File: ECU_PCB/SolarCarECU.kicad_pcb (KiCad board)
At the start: 4 copper layers, 160 x 105.4 mm, 185 parts, among them J2 Screw_Terminal_01x08, J3 Screw_Terminal_01x08, J4 Screw_Terminal_01x08, J5 Screw_Terminal_01x08, J6 Screw_Terminal_01x08, J7 Screw_Terminal_01x08, J8 Screw_Terminal_01x08, Q1 QM6015D, Q2 QM6015D, Q3 QM6015D, Q4 QM6015D, Q5 QM6015D, Q6 QM6015D, Q7 QM6015D, U1 Teensy3.6, U10 LM324A, U11 MCP1403, U2 MCP1403, U3 MCP1403, U4 L7805, U5 MCP2562-E-P, U6 MCP2562-E-P, U7 4504, U8 4504, U9 4504

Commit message: laid tracks for fuses in pcb. bypass capacitors are not clearing rats nest for some reason...is this a problem?
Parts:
- removed C1: 470uF, Capacitor_THT:CP_Radial_D13.0mm_P5.00mm
- added F1: Polyfuse, Fuse:Fuse_0603_1608Metric, F.Cu at (184.3, 96.5)
- added F10: Polyfuse, Fuse:Fuse_0603_1608Metric, B.Cu at (127.3, 107.2)
- added F11: Polyfuse, Fuse:Fuse_0603_1608Metric, B.Cu at (124.7, 107.2)
- added F12: Polyfuse, Fuse:Fuse_0603_1608Metric, F.Cu at (122.2, 107.2)
- added F13: Polyfuse, Fuse:Fuse_0603_1608Metric, F.Cu at (119.6, 107.2)
- added F14: Polyfuse, Fuse:Fuse_0603_1608Metric, F.Cu at (117.1, 107.2)
- added F15: Polyfuse, Fuse:Fuse_0603_1608Metric, F.Cu at (114.6, 107.2)
- added F16: Polyfuse, Fuse:Fuse_0603_1608Metric, F.Cu at (110.0, 112.2)
- added F17: Polyfuse, Fuse:Fuse_0603_1608Metric, F.Cu at (112.0, 112.2)
- added F18: Polyfuse, Fuse:Fuse_0603_1608Metric, F.Cu at (110.4, 124.7)
- added F19: Polyfuse, Fuse:Fuse_0603_1608Metric, B.Cu at (142.5, 133.3)
- added F2: Polyfuse, Fuse:Fuse_0603_1608Metric, F.Cu at (184.3, 98.9)
- added F20: Polyfuse, Fuse:Fuse_0603_1608Metric, B.Cu at (145.0, 133.5)
- added F21: Polyfuse, Fuse:Fuse_0603_1608Metric, B.Cu at (147.6, 133.5)
- added F22: Polyfuse, Fuse:Fuse_0603_1608Metric, B.Cu at (156.6, 102.0)
- added F23: Polyfuse, Fuse:Fuse_0603_1608Metric, B.Cu at (151.5, 107.3)
- added F24: Polyfuse, Fuse:Fuse_0603_1608Metric, B.Cu at (153.9, 131.6)
- added F25: Polyfuse, Fuse:Fuse_0603_1608Metric, B.Cu at (146.8, 121.2)
- added F26: Polyfuse, Fuse:Fuse_0603_1608Metric, F.Cu at (110.5, 120.0)
- added F27: Polyfuse, Fuse:Fuse_0603_1608Metric, B.Cu at (123.4, 102.8)
- added F28: Polyfuse, Fuse:Fuse_0603_1608Metric, B.Cu at (126.0, 102.8)
- added F29: Polyfuse, Fuse:Fuse_0603_1608Metric, B.Cu at (126.0, 129.8)
- added F3: Polyfuse, Fuse:Fuse_0603_1608Metric, B.Cu at (165.6, 106.8)
- added F30: Polyfuse, Fuse:Fuse_0603_1608Metric, B.Cu at (123.4, 129.8)
- added F31: Polyfuse, Fuse:Fuse_0603_1608Metric, B.Cu at (120.9, 129.9)
- added F32: Polyfuse, Fuse:Fuse_0603_1608Metric, B.Cu at (118.4, 129.9)
- added F33: Polyfuse, Fuse:Fuse_0603_1608Metric, B.Cu at (128.7, 102.8)
- added F34: Polyfuse, Fuse:Fuse_0603_1608Metric, B.Cu at (131.1, 102.8)
- added F35: Polyfuse, Fuse:Fuse_0603_1608Metric, B.Cu at (133.7, 102.8)
- added F36: Polyfuse, Fuse:Fuse_0603_1608Metric, B.Cu at (159.0, 136.7)
- added F37: Polyfuse, Fuse:Fuse_0603_1608Metric, B.Cu at (162.8, 121.2)
- added F38: Polyfuse, Fuse:Fuse_0603_1608Metric, B.Cu at (178.3, 110.9)
- added F39: Polyfuse, Fuse:Fuse_0603_1608Metric, F.Cu at (166.6, 103.7)
- added F4: Polyfuse, Fuse:Fuse_0603_1608Metric, B.Cu at (155.2, 107.3)
- added F40: Polyfuse, Fuse:Fuse_0603_1608Metric, B.Cu at (160.3, 133.6)
- added F41: Polyfuse, Fuse:Fuse_0603_1608Metric, B.Cu at (157.7, 133.6)
- added F42: Polyfuse, Fuse:Fuse_0603_1608Metric, F.Cu at (180.8, 122.6)
- added F43: Polyfuse, Fuse:Fuse_0603_1608Metric, F.Cu at (180.8, 120.9)
- added F44: Polyfuse, Fuse:Fuse_0603_1608Metric, B.Cu at (150.1, 133.5)
- added F5: Polyfuse, Fuse:Fuse_0603_1608Metric, B.Cu at (156.5, 129.5)
- added F6: Polyfuse, Fuse:Fuse_0603_1608Metric, B.Cu at (151.4, 115.4)
- added F7: Polyfuse, Fuse:Fuse_0603_1608Metric, B.Cu at (134.9, 107.2)
- added F8: Polyfuse, Fuse:Fuse_0603_1608Metric, B.Cu at (132.3, 107.2)
- added F9: Polyfuse, Fuse:Fuse_0603_1608Metric, B.Cu at (129.8, 107.2)
- added R55: 100k, Resistor_SMD:R_0603_1608Metric, B.Cu at (215.6, 87.1)
- added R95: 0, Resistor_SMD:R_0603_1608Metric, F.Cu at (133.5, 129.5)
- C44: moved to B.Cu
- moved C44 24.4 mm to (181.3, 110.1), turned to 0 degrees
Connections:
- net /CS_0 renamed Net-(U1-Pad12)
- net /CS_2 renamed Net-(U1-Pad70)
- net /MISO_0 renamed Net-(U1-Pad13)
- net /MISO_2 renamed Net-(U1-Pad72)
- net /MOSI_0 renamed Net-(U1-Pad14)
- net /MOSI_2 renamed Net-(U1-Pad71)
- net /SCK_2 renamed Net-(U1-Pad73)
- net /USB_D+ renamed Net-(U1-Pad60)
- net /USB_D- renamed Net-(U1-Pad59)
- U1 pad 10: /UART_3_TX -> Net-(F6-Pad1)
- U1 pad 16: /LV_HAZARD_CTRL -> Net-(F7-Pad1)
- U1 pad 17: /LV_HAZARD_LED -> Net-(F8-Pad1)
- U1 pad 18: /LV_DOWN_CTRL -> Net-(F9-Pad1)
- U1 pad 19: /LV_UP_CTRL -> Net-(F10-Pad1)
- U1 pad 2: /UART_1_RX -> Net-(F1-Pad1)
- U1 pad 20: /LV_SEL_CTRL -> Net-(F11-Pad1)
- U1 pad 21: /CAN0_TX -> Net-(F12-Pad1)
- U1 pad 22: /CAN0_RX -> Net-(F13-Pad1)
- U1 pad 23: /UART_4_RX -> Net-(F14-Pad1)
- U1 pad 24: /UART_4_TX -> Net-(F15-Pad1)
- U1 pad 3: /UART_1_TX -> Net-(F2-Pad1)
- U1 pad 30: /CAN1_TX -> Net-(F16-Pad1)
- U1 pad 31: /CAN1_RX -> Net-(F17-Pad1)
- U1 pad 36: /LV_MOTOR_R_ECO_EN -> Net-(F18-Pad1)
- U1 pad 4: /LV_KILL_SENSE -> Net-(F3-Pad1)
- U1 pad 41: /LV_GEARSHIFT_CTRL -> Net-(F19-Pad1)
- U1 pad 42: /LV_TURNSIG_CTRL -> Net-(F20-Pad1)
- U1 pad 43: /LV_THROTTLE_CTRL -> Net-(F21-Pad1)
- U1 pad 44: /LV_REGEN_CTRL -> Net-(F44-Pad2)
- U1 pad 45: /SDA_0 -> Net-(F43-Pad2)
- U1 pad 46: /SCL_0 -> Net-(F42-Pad2)
- U1 pad 47: /LV_BRAKE_CTRL -> Net-(F41-Pad2)
- U1 pad 48: /LV_STEER_CTRL -> Net-(F40-Pad2)
- U1 pad 49: /LV_HORN_CTRL -> Net-(F39-Pad2)
- U1 pad 50: /LV_HEADLIGHT_CTRL -> Net-(F38-Pad2)
- U1 pad 56: /LV_MOTOR_R_METER -> Net-(F37-Pad2)
- U1 pad 57: /LV_MOTOR_L_METER -> Net-(F36-Pad2)
- U1 pad 67: /LV_LEFT_BLINKERS -> Net-(F35-Pad2)
- U1 pad 68: /LV_RIGHT_BLINKERS -> Net-(F34-Pad2)
- U1 pad 69: /LV_HEADLIGHTS -> Net-(F33-Pad2)
- U1 pad 76: /UART_6_RX -> Net-(F32-Pad2)
- U1 pad 77: /UART_6_TX -> Net-(F31-Pad2)
- U1 pad 78: /LV_MOTOR_L_ECO_EN -> Net-(F30-Pad2)
- U1 pad 79: /LV_MOTOR_L_REGEN_EN -> Net-(F29-Pad2)
- U1 pad 8: /LV_STROBE -> Net-(F4-Pad1)
- U1 pad 80: /LV_MOTOR_R_REV_EN -> Net-(F28-Pad2)
- U1 pad 81: /LV_MOTOR_R_FWD_EN -> Net-(F27-Pad2)
- U1 pad 82: /LV_MOTOR_R_REGEN_EN -> Net-(F26-Pad2)
- U1 pad 83: /LV_MOTOR_L_REV_EN -> Net-(F25-Pad2)
- U1 pad 84: /LV_MOTOR_L_FWD_EN -> Net-(F24-Pad2)
- U1 pad 85: /LV_BRAKELIGHTS -> Net-(F23-Pad2)
- U1 pad 86: /LV_HORN -> Net-(F22-Pad2)
- U1 pad 9: /UART_3_RX -> Net-(F5-Pad1)
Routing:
- net Net-(F43-Pad2): track 0.00 -> 29.6 mm
- net /SDA_0: track 124.1 -> 96.1 mm
- net /LV_MOTOR_R_FWD_EN: track 79.7 -> 51.8 mm
- net /LV_MOTOR_R_REGEN_EN: track 67.1 -> 40.4 mm
- net /SCL_0: track 121.1 -> 94.6 mm
- net Net-(F42-Pad2): track 0.00 -> 26.4 mm
- net Net-(F27-Pad2): track 0.00 -> 26.4 mm
- net Net-(F26-Pad2): track 0.00 -> 26.1 mm
- net /LV_HEADLIGHT_CTRL: track 81.2 -> 55.5 mm, vias 3 -> 1
- net /LV_HORN_CTRL: track 83.0 -> 58.0 mm, vias 3 -> 2
- net Net-(F39-Pad2): track 0.00 -> 23.4 mm, vias 0 -> 1
- net /UART_1_RX: track 49.9 -> 27.0 mm, vias 1 -> 0
- net Net-(F38-Pad2): track 0.00 -> 22.3 mm, vias 0 -> 2
- net /UART_1_TX: track 49.1 -> 27.1 mm
- net /LV_MOTOR_R_REV_EN: track 77.5 -> 56.1 mm
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
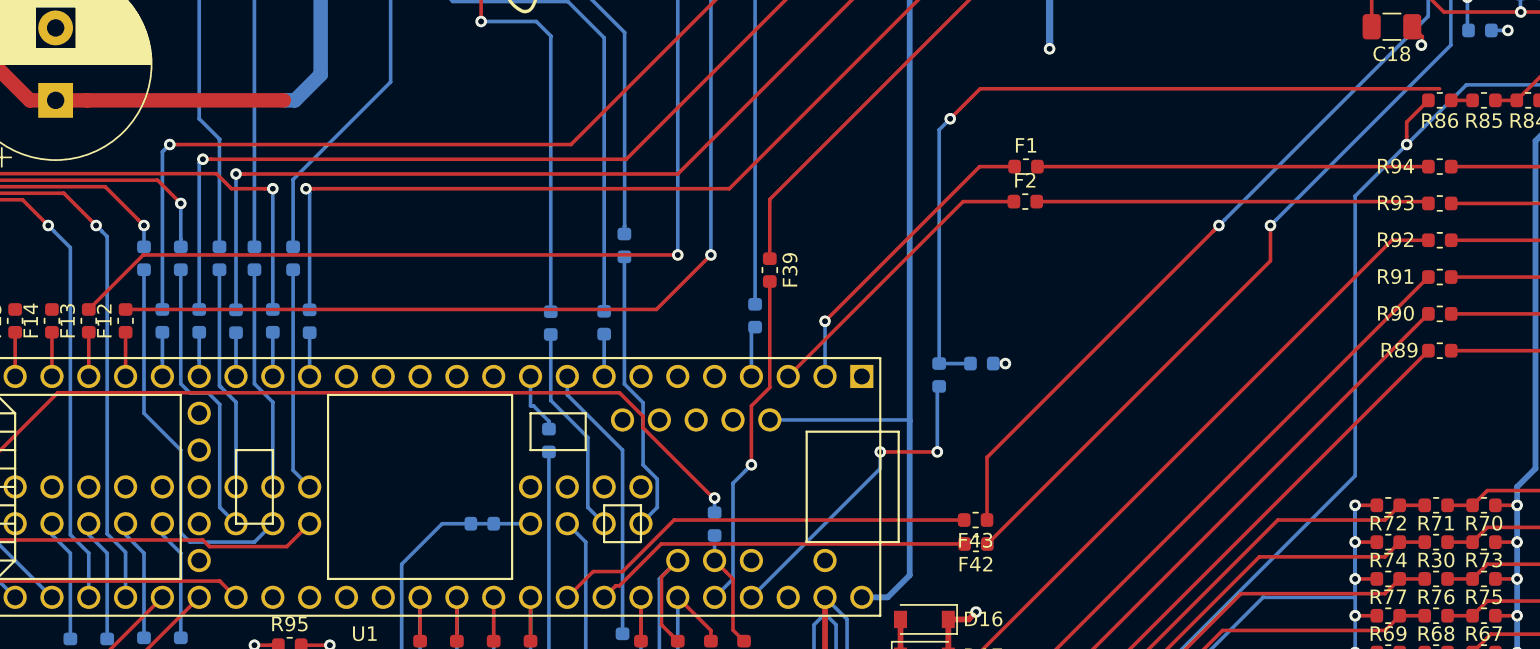
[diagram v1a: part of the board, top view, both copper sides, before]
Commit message: fix a couple traces
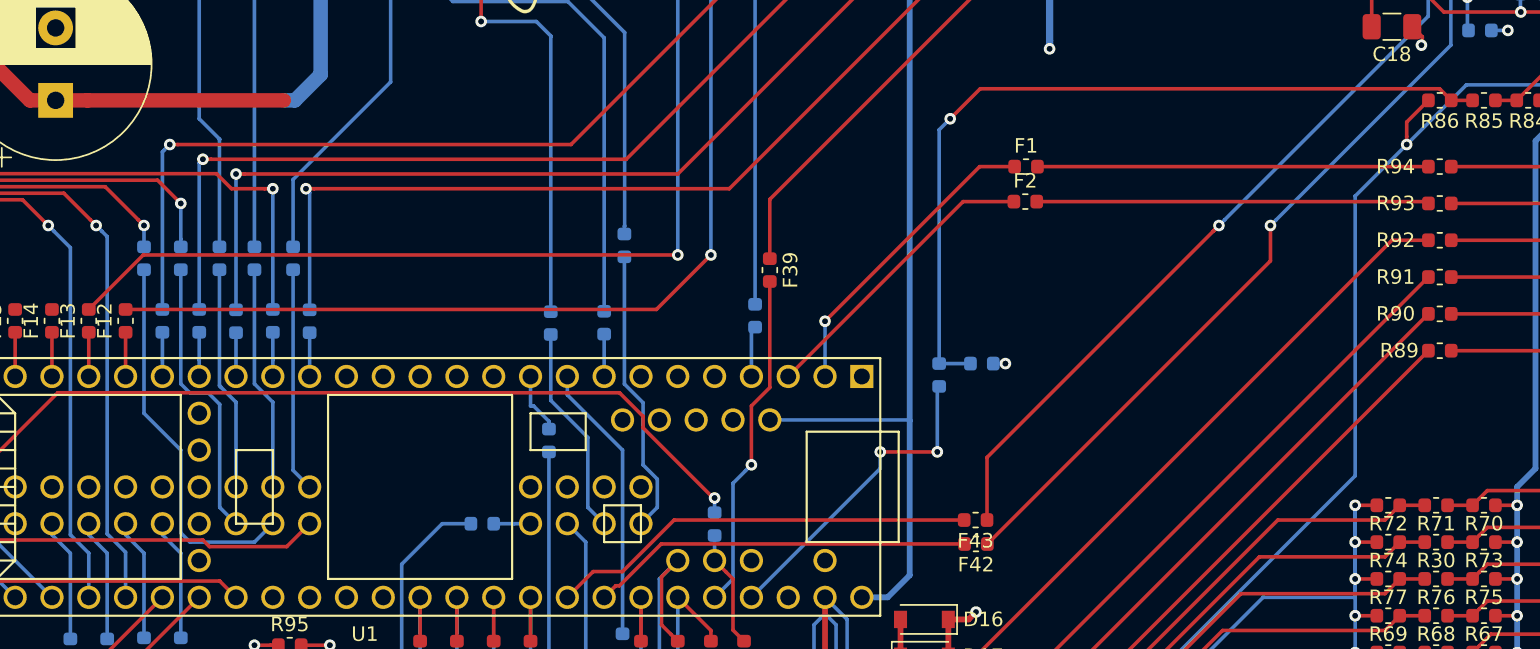
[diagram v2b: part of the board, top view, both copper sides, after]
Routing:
- net /LV_MOTOR_L_REV_EN: track 81.3 -> 77.2 mm
- net Net-(F25-Pad2): track 0.00 -> 2.54 mm
- net /LV_HEADLIGHT_CTRL: track 55.5 -> 56.6 mm
- net Net-(F13-Pad1): track 2.54 -> 3.05 mm
- net Net-(F12-Pad1): track 2.54 -> 3.05 mm

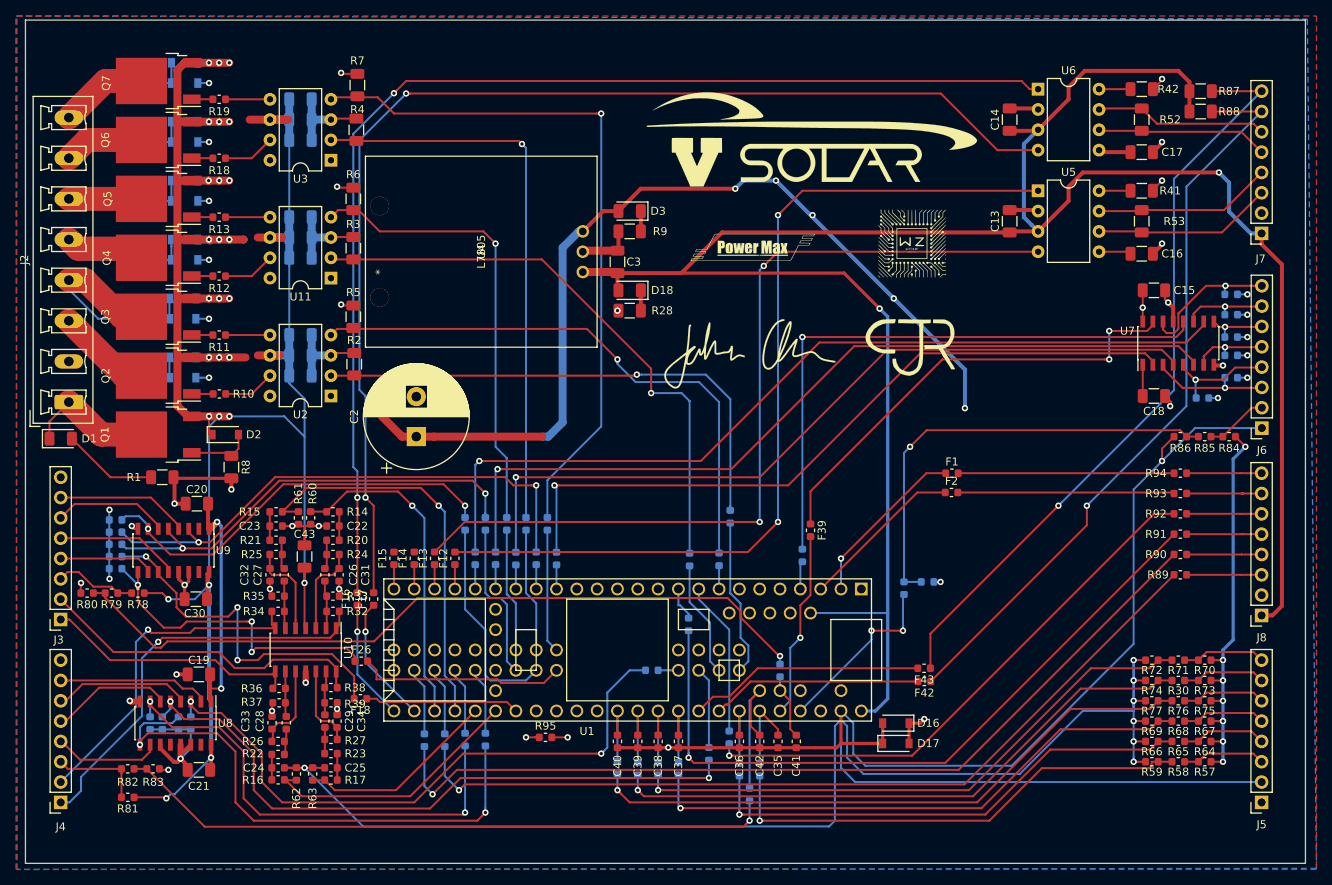
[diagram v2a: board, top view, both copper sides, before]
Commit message: fixed drc and routing errors
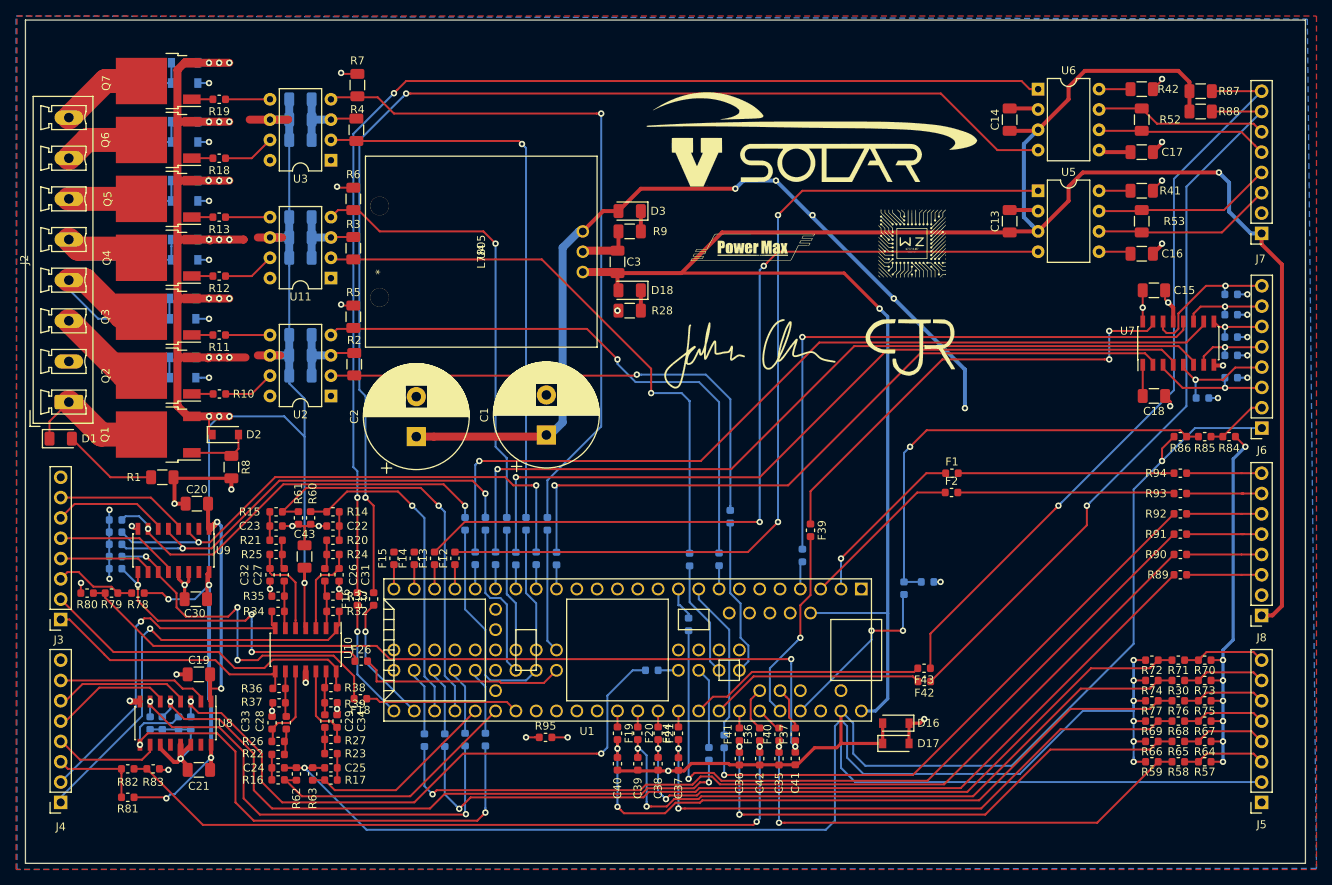
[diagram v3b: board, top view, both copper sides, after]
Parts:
- added C1: 470uF, Capacitor_THT:CP_Radial_D13.0mm_P5.00mm, F.Cu at (133.6, 91.7)
- F19, F20, F21, F36, F37, F40, F41, F44: moved to F.Cu
- moved F37 8.20 mm to (164.7, 129.2), turned to 90 degrees
- moved F36 7.63 mm to (160.3, 129.2)
- moved F40 5.04 mm to (162.7, 129.2)
- moved F20 4.42 mm to (145.0, 129.0)
- moved F21 4.42 mm to (147.6, 129.0)
- moved F41 4.42 mm to (157.7, 129.2)
- moved F44 4.42 mm to (150.1, 129.0)
- moved F19 4.29 mm to (142.5, 129.0)
- moved C37 2.82 mm to (150.1, 132.9)
- moved C38 2.79 mm to (147.6, 132.8)
- moved C39 2.79 mm to (145.0, 132.8)
- moved C40 2.79 mm to (142.5, 132.8)
- moved C35 2.16 mm to (162.7, 132.2)
- moved C36 2.16 mm to (157.7, 132.2)
- moved C42 2.16 mm to (160.3, 132.2)
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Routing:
- net Net-(F36-Pad2): track 12.7 -> 5.61 mm
- net /LV_GEARSHIFT_CTRL: track 80.3 -> 87.1 mm, vias 1 -> 2
- net +12V: track 446.5 -> 441.2 mm
- net /LV_TURNSIG_CTRL: track 78.0 -> 83.0 mm, vias 1 -> 2
- net Net-(F44-Pad2): track 6.43 -> 2.01 mm
- net Net-(F21-Pad1): track 6.43 -> 2.13 mm
- net Net-(F20-Pad1): track 6.43 -> 2.13 mm
- net Net-(F41-Pad2): track 6.55 -> 2.39 mm
- net Net-(F19-Pad1): track 6.30 -> 2.13 mm
- net /UART_3_TX: track 88.7 -> 92.7 mm
- net Net-(F37-Pad2): track 1.73 -> 5.46 mm
- net /UART_3_RX: track 69.6 -> 73.2 mm
- net /LV_THROTTLE_CTRL: track 75.9 -> 79.3 mm, vias 1 -> 2
- net /UART_6_TX: track 106.7 -> 110.0 mm
- net Net-(F40-Pad2): track 6.55 -> 3.30 mm
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
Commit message: clean up some traces
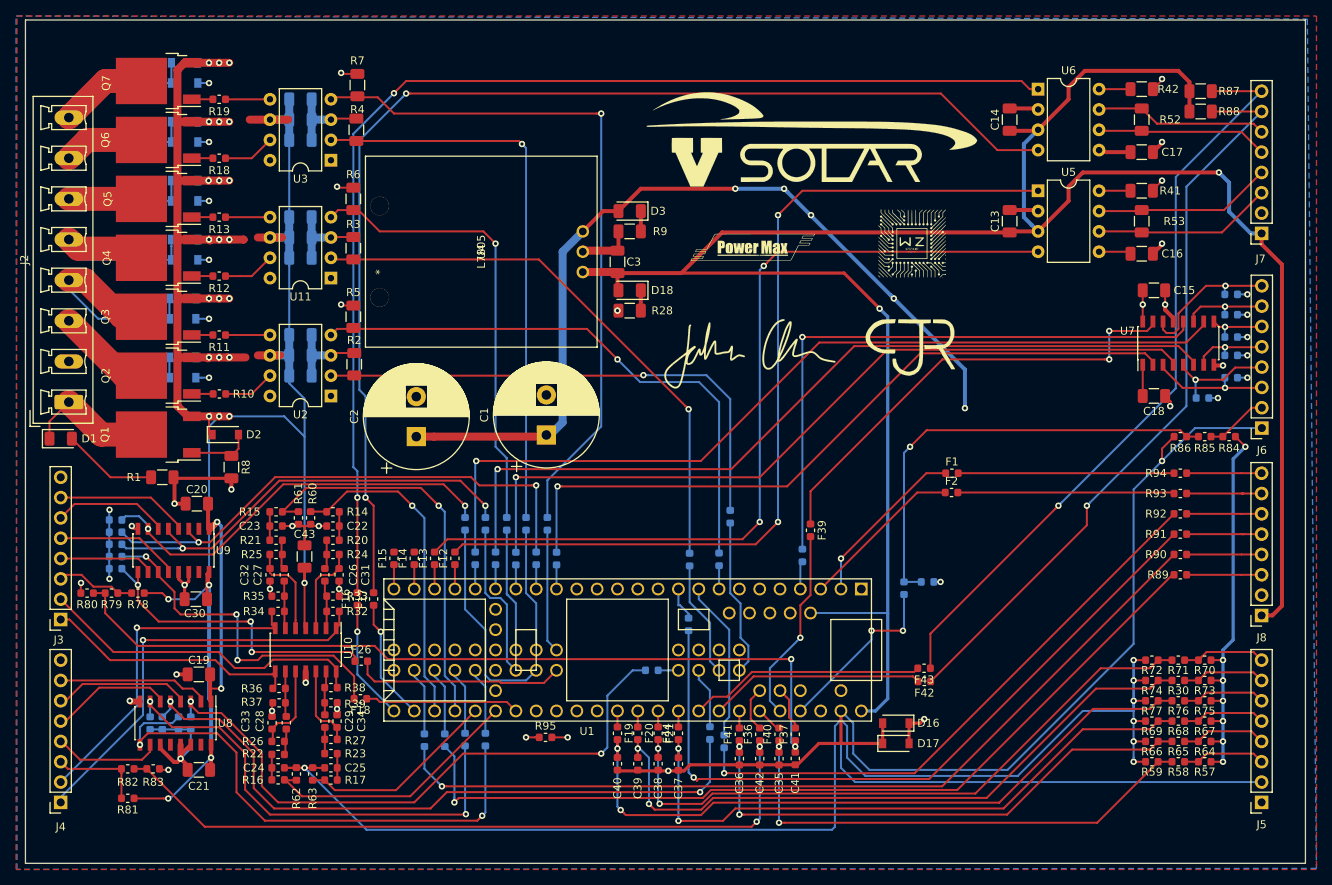
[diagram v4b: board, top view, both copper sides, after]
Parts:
- moved F24 2.59 mm to (154.1, 129.0)
- moved R81 0.13 mm to (81.3, 137.2)
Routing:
- net /UART_6_RX: track 112.3 -> 109.4 mm
- net /LV_MOTOR_L_FWD_EN: track 82.3 -> 84.8 mm
- net Net-(F24-Pad2): track 10.2 -> 7.64 mm
- net /LV_BRAKELIGHTS: track 73.1 -> 70.6 mm
- net /LV_REGEN_CTRL: track 75.9 -> 78.0 mm
- net /MOTOR_L_THROTTLE: track 53.3 -> 51.8 mm
- net /LV_MOTOR_R_ECO_EN: track 44.9 -> 43.5 mm
- net /LV_THROTTLE_CTRL: track 79.3 -> 80.6 mm
- net /LV_MOTOR_R_REGEN_EN: track 40.4 -> 39.2 mm
- net /LV_MOTOR_R_METER: track 104.3 -> 105.4 mm
- net +12V: track 441.2 -> 440.0 mm
- net /MOTOR_L_REGEN: track 44.0 -> 42.9 mm
- net /UART_3_TX: track 92.7 -> 91.6 mm
- net /LV_GEARSHIFT_CTRL: track 87.1 -> 86.0 mm
- net GNDA: track 377.8 -> 378.7 mm
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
